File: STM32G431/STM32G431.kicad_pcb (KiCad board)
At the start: 4 copper layers, 60 x 44 mm, 154 parts, among them J1 W, J10 NTC, J11 LED, J2 U, J3 V, J4 GND, J5 VIN, J6 UART, J8 HALL, J9 AIN/PWM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

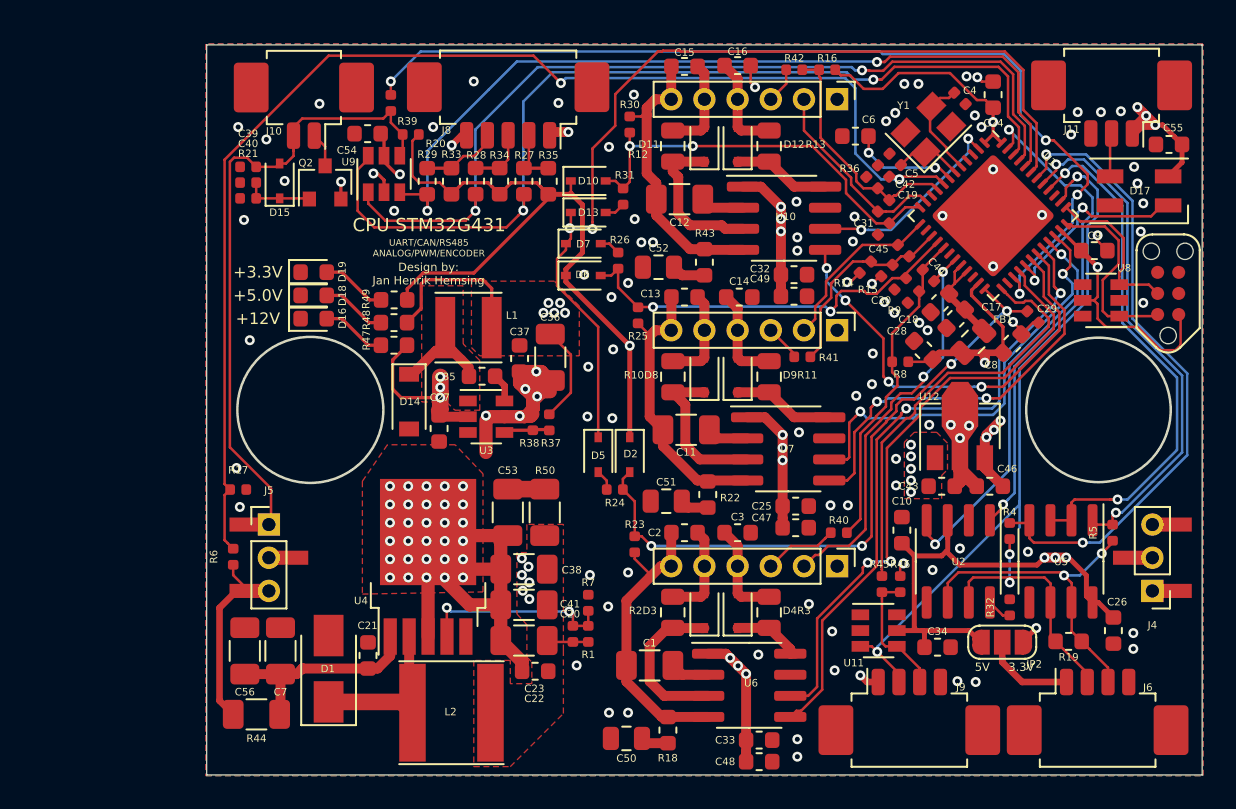
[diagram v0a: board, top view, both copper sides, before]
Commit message: updated layout
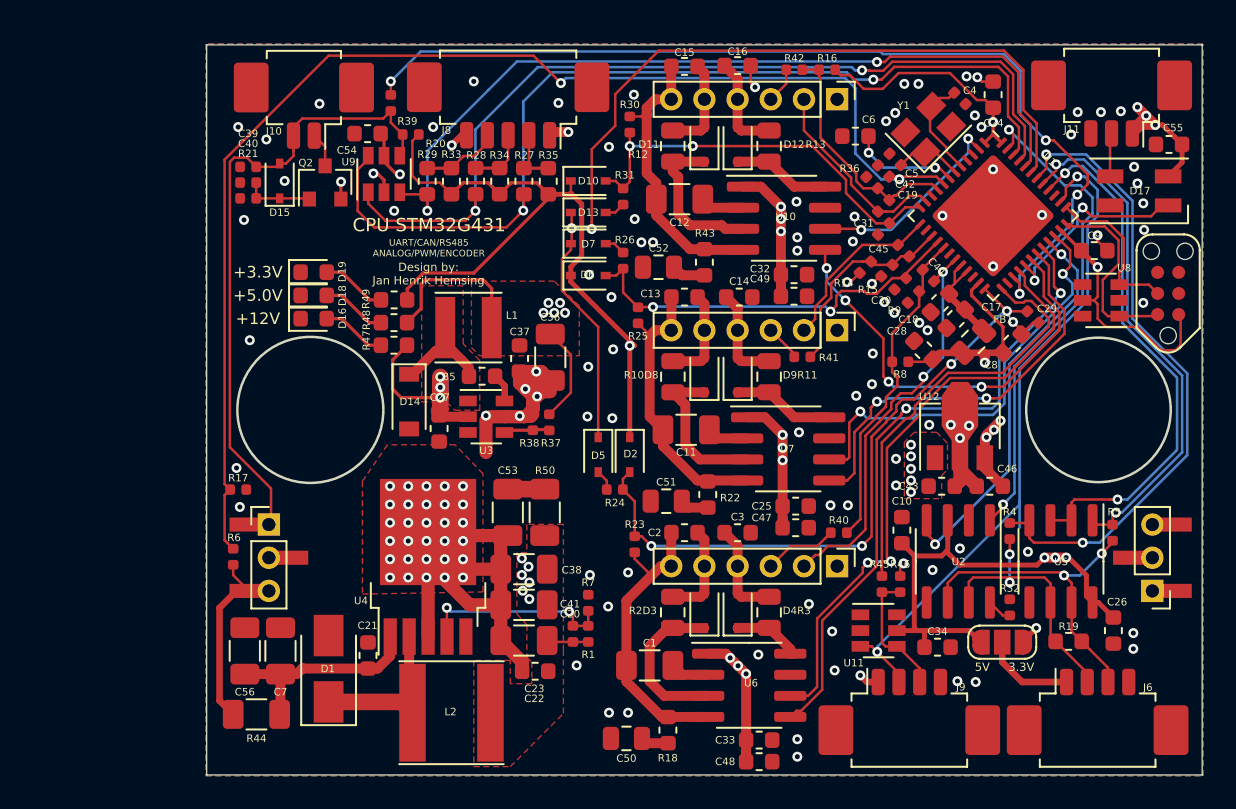
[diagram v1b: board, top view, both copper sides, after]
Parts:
- moved D7 0.30 mm to (43.0, 35.0)
- moved R26 0.30 mm to (45.1, 36.0)
- moved D6 0.30 mm to (43.0, 36.9)
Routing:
- net GND: vias 127 -> 126

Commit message: updated layout
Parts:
- added C57: 10u, Capacitor_SMD:C_1206_3216Metric, F.Cu at (11.6, 45.0)
- added C58: 10u, Capacitor_SMD:C_1206_3216Metric, F.Cu at (42.7, 41.8)
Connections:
- C43 pad 1: +12V -> +5V
- U12 pad 1: +12V -> +5V
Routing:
- net +12V: track 144.3 -> 116.2 mm, vias 23 -> 18
- net +5V: track 150.9 -> 153.8 mm
- net GND: track 69.3 -> 71.3 mm, vias 126 -> 131
- net UL: track 36.6 -> 35.8 mm
- net GPIO_BEMF: track 57.6 -> 58.4 mm
- net Ain: track 25.4 -> 26.1 mm
- net UH: vias 2 -> 4

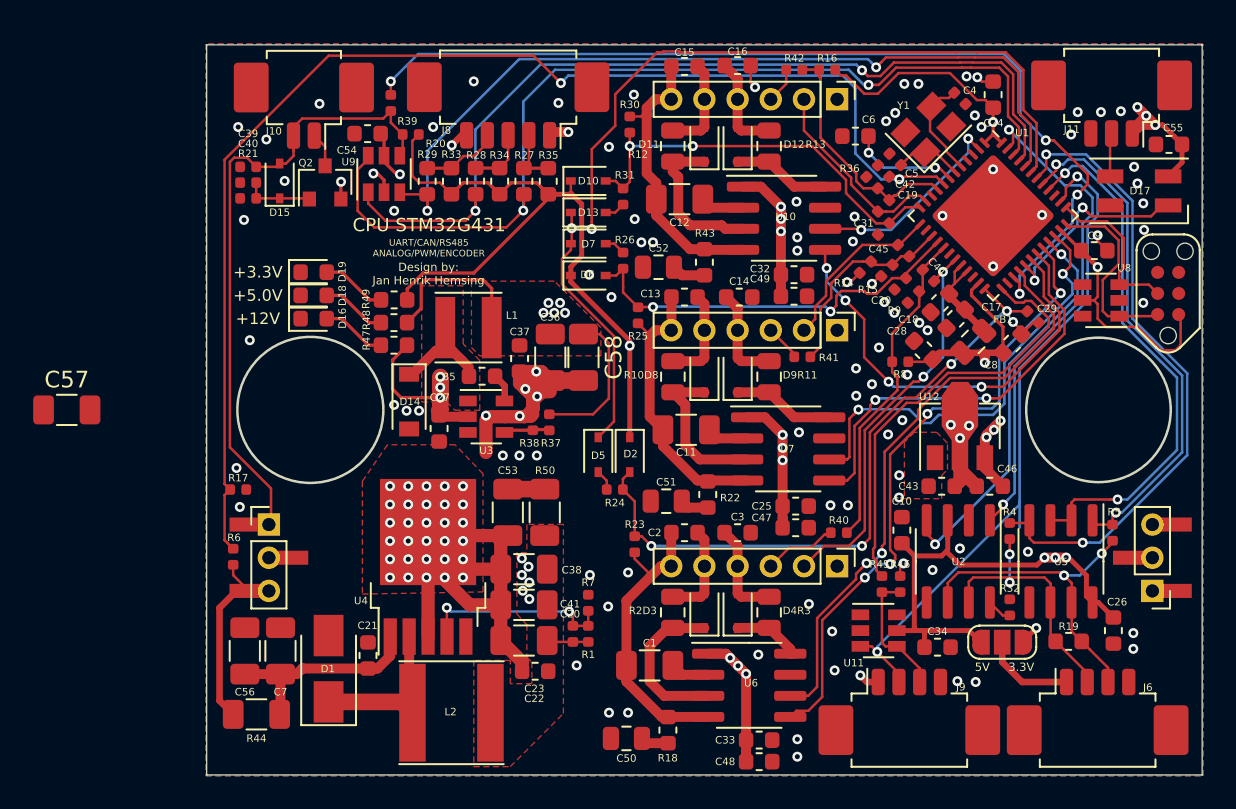
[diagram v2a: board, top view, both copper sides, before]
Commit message: updated layout
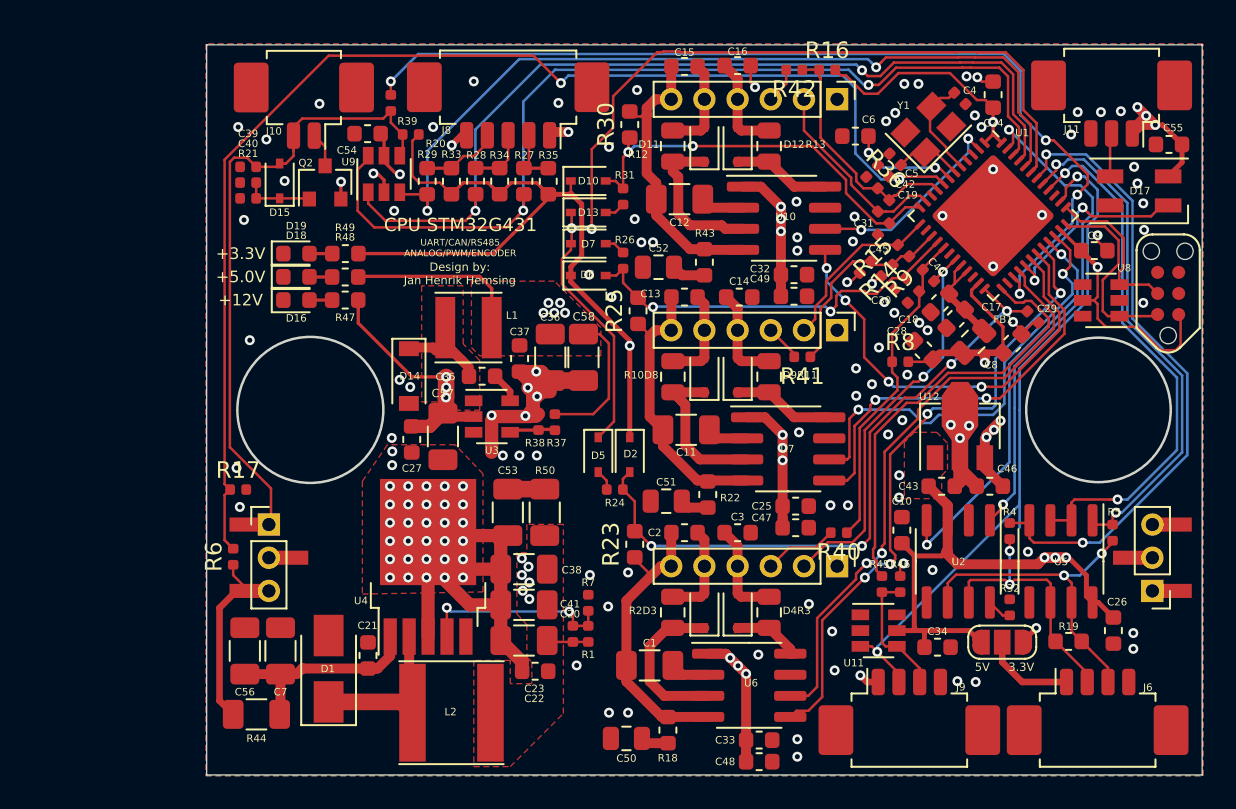
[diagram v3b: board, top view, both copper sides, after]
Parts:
- R14, R15, R16, R17, R36, R40, R41, R42, R6, R8, R9: footprint Capacitor_SMD:C_0402_1005Metric -> Resistor_SMD:R_0402_1005Metric
- R23, R25, R30: footprint Resistor_SMD:R_0402_1005Metric -> Resistor_SMD:R_0603_1608Metric
- moved C57 22.7 mm to (34.2, 46.6), turned to 270 degrees
- moved R49 4.05 mm to (28.4, 35.6)
- moved R48 4.03 mm to (28.4, 37.0)
- moved R47 4.01 mm to (28.4, 38.4)
- moved C27 1.78 mm to (32.4, 46.8)
- moved D14 1.54 mm to (32.2, 43.0)
- moved D18 1.53 mm to (25.4, 37.0)
- moved D19 1.53 mm to (25.4, 35.6)
- moved D16 1.53 mm to (25.4, 38.4)
- moved R38 0.34 mm to (40.0, 45.7)
- moved R37 0.34 mm to (41.0, 45.7)
- moved U3 0.34 mm to (37.2, 45.4)
- moved R25 0.27 mm to (46.0, 39.0)
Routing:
- net +5V: track 153.8 -> 161.6 mm
- net Net-(D16-Pad2): track 3.95 -> 1.36 mm
- net Net-(D19-Pad2): track 3.95 -> 1.38 mm
- net Net-(D18-Pad2): track 3.93 -> 1.37 mm
- net +12V: track 116.2 -> 118.7 mm
- net +3V3: track 175.8 -> 177.6 mm
- net GND: track 71.3 -> 70.2 mm, vias 131 -> 132
- net Net-(C35-Pad2): track 4.68 -> 4.12 mm
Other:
- net class Default: clearance 0.154 -> 0.12
- rule trace_clearance: 0.154 -> 0.12

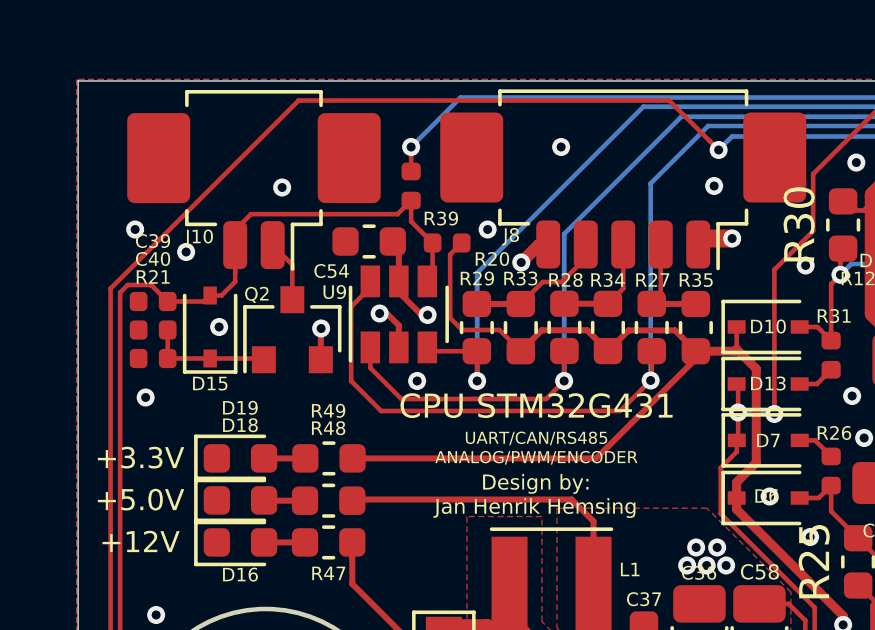
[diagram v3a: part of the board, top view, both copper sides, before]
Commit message: updated layout
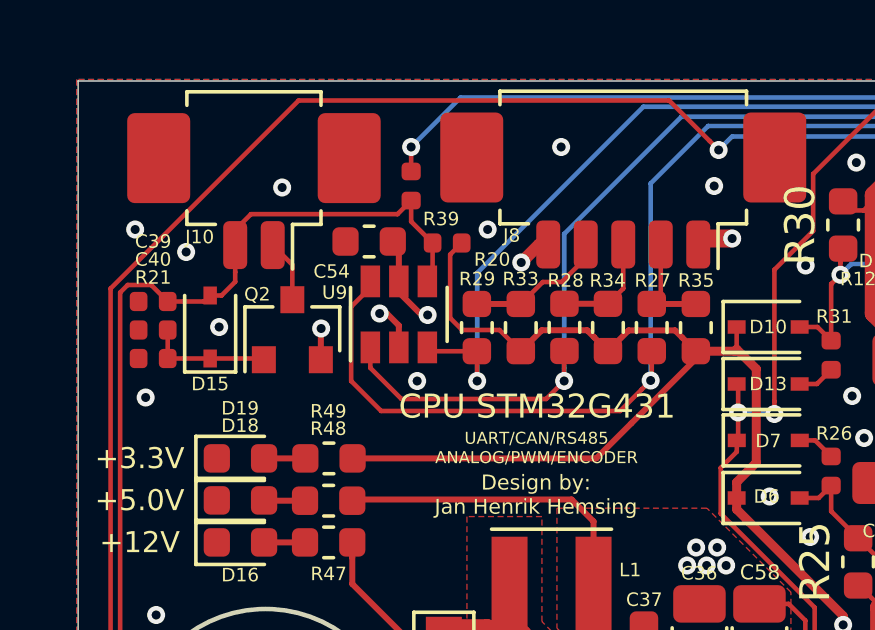
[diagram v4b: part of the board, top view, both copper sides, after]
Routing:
- added copper zone on In2.Cu, net +12V
- added copper zone on In2.Cu, net +3V3
- added copper zone on In2.Cu, net +5V
- added copper zone on In1.Cu, net GND
- removed copper zone on In1.Cu, net +12V
- removed copper zone on In1.Cu, net +5V
- removed copper zone on In2.Cu, net GND
